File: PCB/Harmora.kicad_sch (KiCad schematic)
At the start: 14 parts, among them U14 ATmega328p-AU, U17 128x64 2.42 inc, Y1 16Mhz

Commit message: new schematics
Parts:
- added C50: 100nF, Footprints:0603_C, symbol Symbols:Capacitor 0603
- added FB1: 600Ω@100MHz, Footprints:0603_FB, symbol Symbols:Ferrite_beat
- C44, C45, C46, C47, C48: footprint (none) -> Footprints:0603_C
- C49: value 12pF -> 100nF; footprint (none) -> Footprints:0603_C
- R10, R11, R12, R13, R9: footprint (none) -> Footprints:0603_R
- U14: footprint (none) -> Footprints:ATMEGA328P-AU
- U17: footprint (none) -> Footprints:SPI Screen PinHeader
- Y1: footprint (none) -> Footprints:Crystal Oscillator 16MHz
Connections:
- net GND: now also C49.1, C50.1
- net VCC: now also FB1.1; no longer C45.2, C46.2, C49.1, U14.18 (AVCC), U14.4 (VCC)
- new net: C45.2, C46.2, FB1.2, U14.18 (AVCC)
- new net: C50.2, U14.4 (VCC)
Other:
- sheet ATmega32u4: file MCU_32u4.kicad_sch -> schematic_pages/MCU_32u4.kicad_sch
- note added: "Crystal oscilator"
- note removed: "Crystal"
- moved on the sheet: C45, C46, C47, C48, C49, Y1

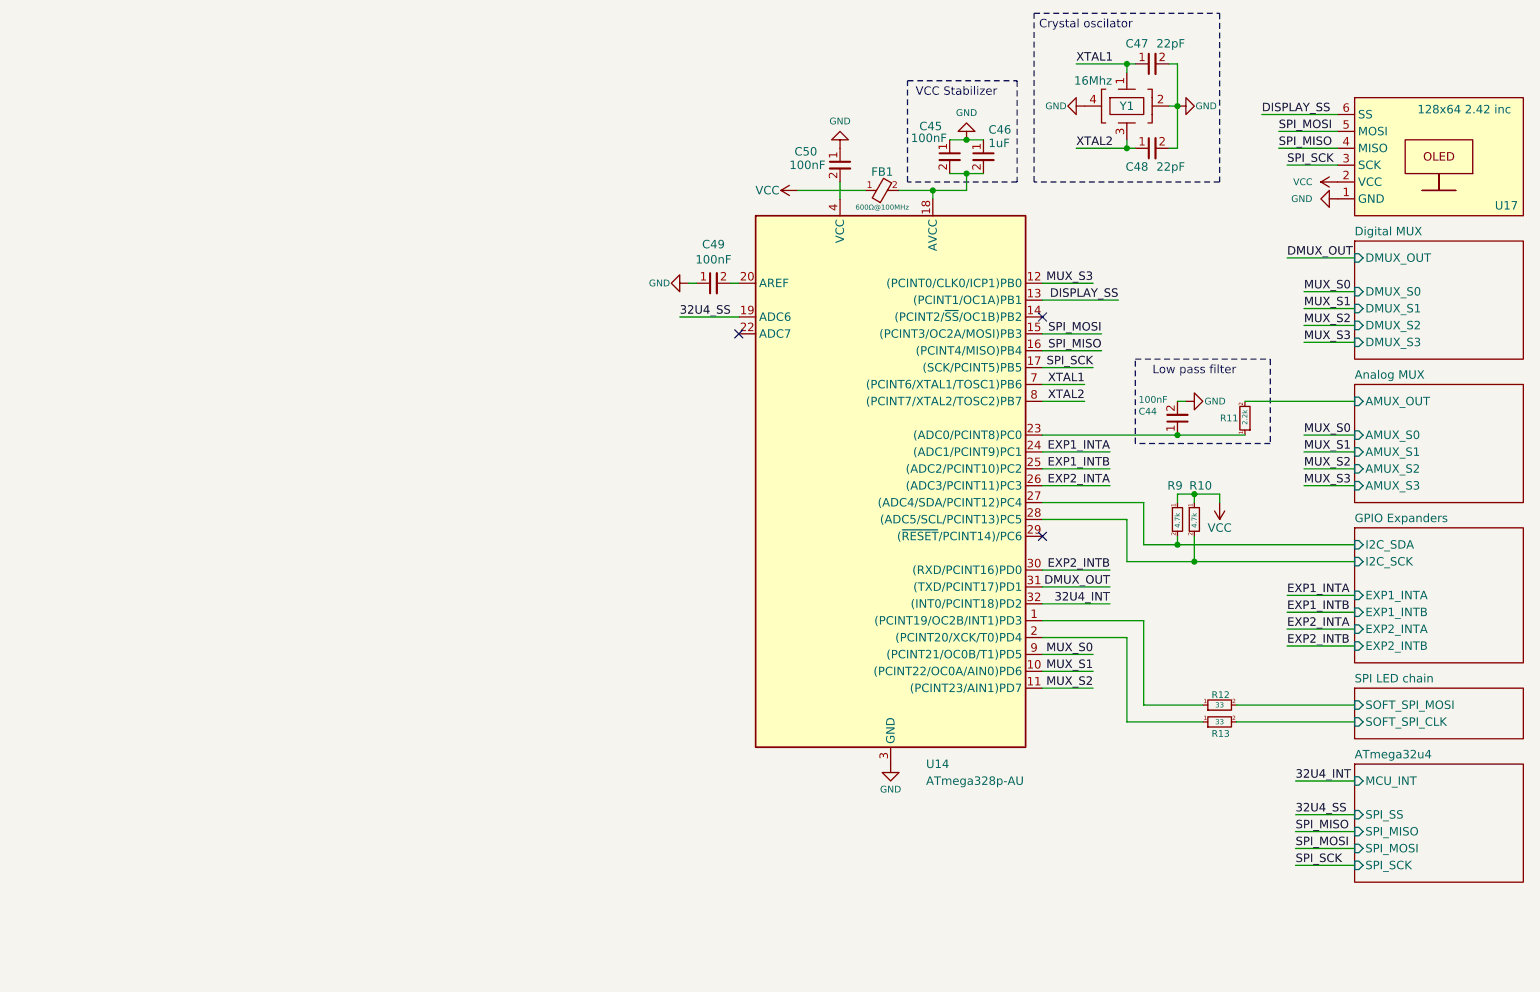
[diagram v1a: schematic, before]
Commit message: ISP ports, RESET lines, MIDI DIN 5
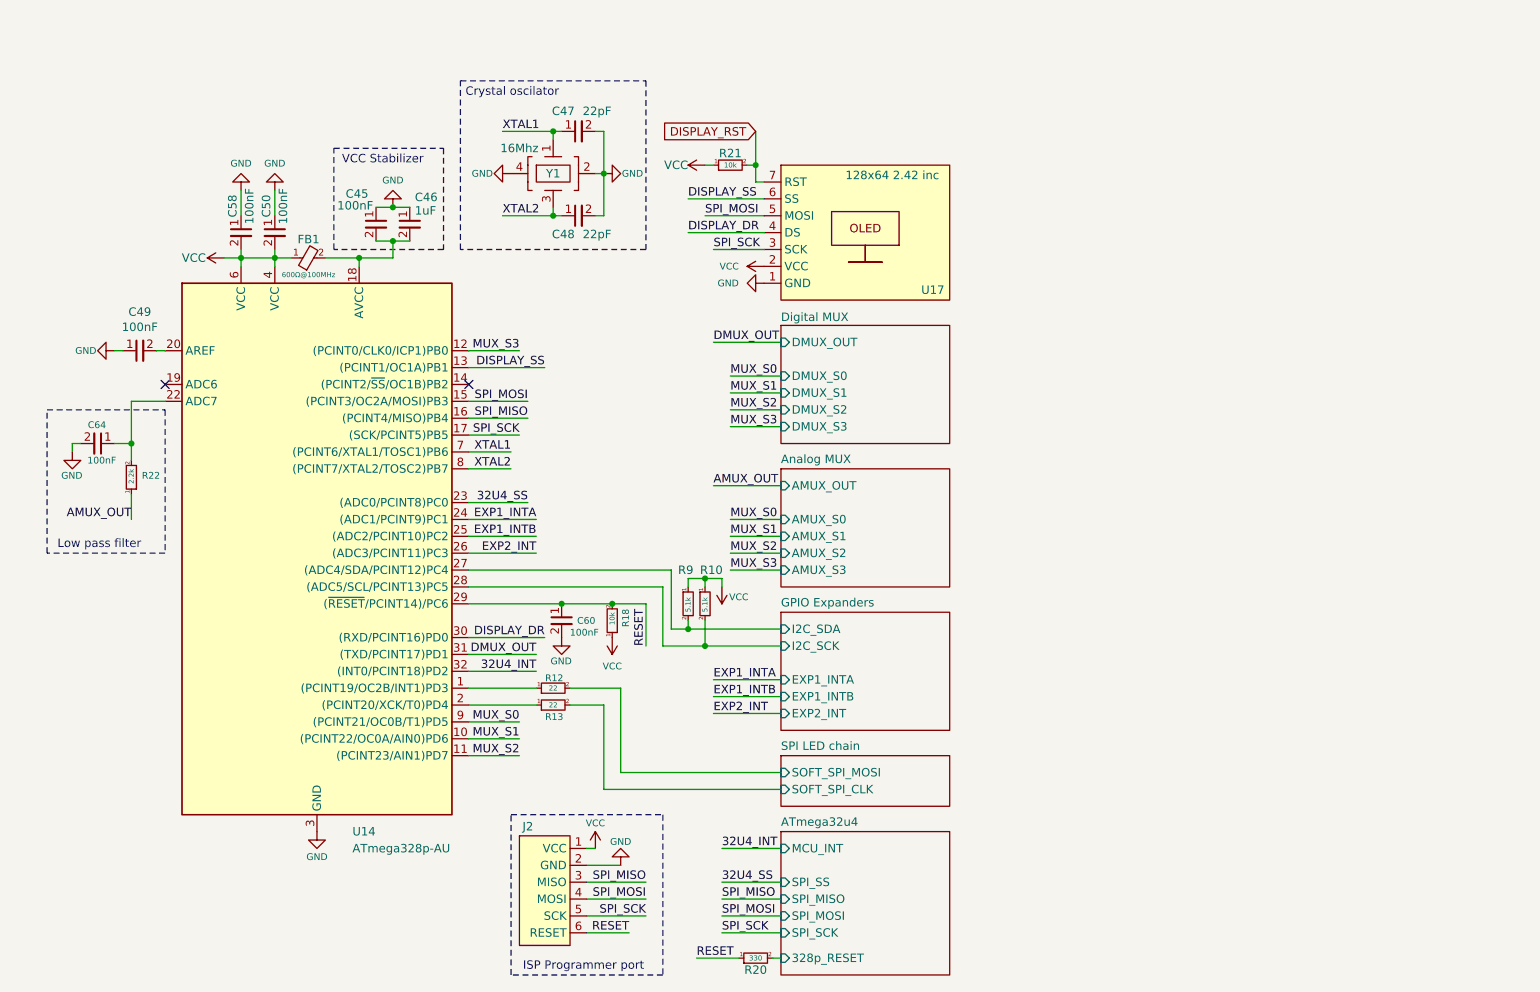
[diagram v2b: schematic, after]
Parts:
- removed C44: 100nF, Footprints:0603_C, symbol Symbols:Capacitor 0603
- removed R11: 2.2k, Footprints:0603_R, symbol Symbols:Resistor 0603
- added C58, C60, C64: 100nF, Footprints:0603_C, symbol Symbols:Capacitor 0603
- added J2: ~, Footprints:ISP port, symbol Symbols:ISP_Port
- added R18, R21: 10k, Footprints:0603_R, symbol Symbols:Resistor 0603
- added R20: 330, Footprints:0603_R, symbol Symbols:Resistor 0603
- added R22: 2.2k, Footprints:0603_R, symbol Symbols:Resistor 0603
- R10, R9: value 4.7k -> 5.1k
- R12, R13: value 33 -> 22
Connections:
- net 32U4_SS: now also U14.23 ((ADC0/PCINT8)PC0); no longer U14.19 (ADC6)
- net GND: now also C58.1, C60.2, C64.2, J2.2 (GND)
- net SPI_MISO: now also J2.3 (MISO); no longer U17.4 (MISO)
- net SPI_MOSI: now also J2.4 (MOSI)
- net SPI_SCK: now also J2.5 (SCK)
- net VCC: now also C50.2, U14.4 (VCC), U14.6 (VCC), C58.2, J2.1 (VCC), R18.1, R21.1
- net at U14.22 (ADC7): now also C64.1, R22.2
- net RESET: now reaches U14.29 ((~{RESET}/PCINT14)/PC6)
- net RESET: now also C60.1, J2.6 (RESET), R18.2, R20.1
- net EXP2_INTA renamed EXP2_INT
- net EXP2_INTB renamed DISPLAY_DR
- net DISPLAY_DR: now also U17.4 (DS)
- new net AMUX_OUT: R22.1
- new net ATmega32u4/328p_RESET: R20.2
- new net DISPLAY_RST: R21.2, U17.7 (RST)
- no-connect marks 3 -> 2
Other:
- sheet ATmega32u4 ports: added 328p_RESET; removed none
- sheet GPIO Expanders ports: added EXP2_INT; removed EXP2_INTA, EXP2_INTB
- note added: "ISP Programmer port"
- moved on the sheet: C45, C46, C47, C48, C49, C50, FB1, R10, R12, R13, R9, Y1

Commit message: led chain
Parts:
- renumbered U17 to J5
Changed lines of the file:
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@@
 		(on_board yes)
 		(dnp no)
-		(property "Reference" "U17"
+		(property "Reference" "J5"
 			(at 152.4 63.246 0)
 			(effects
@@
 			(project "MCU_328p"
 				(path "/de43e009-b04c-42c1-b131-cdc664039a0d"
-					(reference "U17")
+					(reference "J5")
 					(unit 1)
 				)

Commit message: pcb: piano done
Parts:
- renumbered C46 to C73, C47 to C79, C48 to C80, R12 to R10, R13 to R11, R18 to R14, R21 to R16, R20 to R17, R22 to R5, R9 to R6, R10 to R7
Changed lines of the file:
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@@
 		(on_board yes)
 		(dnp no)
-		(property "Reference" "R13"
+		(property "Reference" "R11"
 			(at 96.774 127.508 90)
 			(effects
@@
 			(project "pcb_schematics"
 				(path "/de43e009-b04c-42c1-b131-cdc664039a0d"
-					(reference "R13")
+					(reference "R11")
 					(unit 1)
 				)
@@
 		(on_board yes)
 		(dnp no)
-		(property "Reference" "C47"
+		(property "Reference" "C79"
 			(at 96.774 36.322 90)
 			(effects
@@
 			(project ""
 				(path "/de43e009-b04c-42c1-b131-cdc664039a0d"
-					(reference "C47")
+					(reference "C79")
 					(unit 1)
 				)
@@
 		(on_board yes)
 		(dnp no)
-		(property "Reference" "C48"
+		(property "Reference" "C80"
 			(at 96.774 54.864 90)
 			(effects
@@
 			(project "MCU_328p"
 				(path "/de43e009-b04c-42c1-b131-cdc664039a0d"
-					(reference "C48")
+					(reference "C80")
 					(unit 1)
 				)
@@
 		(on_board yes)
 		(dnp no)
-		(property "Reference" "C46"
+		(property "Reference" "C73"
 			(at 74.422 49.2822 0)
 			(effects
@@
 			(project "pcb_schematics"
 				(path "/de43e009-b04c-42c1-b131-cdc664039a0d"
-					(reference "C46")
+					(reference "C73")
 					(unit 1)
 				)
@@
 		(on_board yes)
 		(dnp no)
-		(property "Reference" "R12"
+		(property "Reference" "R10"
 			(at 96.774 121.666 90)
 			(effects
@@
 			(project "pcb_schematics"
 				(path "/de43e009-b04c-42c1-b131-cdc664039a0d"
-					(reference "R12")
+					(reference "R10")
 					(unit 1)
 				)
@@
 		(on_board yes)
 		(dnp no)
-		(property "Reference" "R10"
+		(property "Reference" "R7"
 			(at 117.348 105.41 0)
 			(effects
@@
 			(project "pcb_schematics"
 				(path "/de43e009-b04c-42c1-b131-cdc664039a0d"
-					(reference "R10")
+					(reference "R7")
 					(unit 1)
 				)
@@
 		(on_board yes)
 		(dnp no)
-		(property "Reference" "R18"
+		(property "Reference" "R14"
 			(at 106.172 111.252 90)
 			(effects
@@
 			(project "Harmora"
 				(path "/de43e009-b04c-42c1-b131-cdc664039a0d"
-					(reference "R18")
+					(reference "R14")
 					(unit 1)
 				)
@@
 		(on_board yes)
 		(dnp no)
-		(property "Reference" "R20"
+		(property "Reference" "R17"
 			(at 125.73 165.608 90)
 			(effects
@@
 			(project "Harmora"
 				(path "/de43e009-b04c-42c1-b131-cdc664039a0d"
-					(reference "R20")
+					(reference "R17")
 					(unit 1)
 				)
@@
 		(on_board yes)
 		(dnp no)
-		(property "Reference" "R22"
-			(at 36.068 91.186 0)
+		(property "Reference" "R5"
+			(at 35.052 91.44 0)
 			(effects
 				(font
@@
 			(project "Harmora"
 				(path "/de43e009-b04c-42c1-b131-cdc664039a0d"
-					(reference "R22")
+					(reference "R5")
 					(unit 1)
 				)
@@
 		(on_board yes)
 		(dnp no)
-		(property "Reference" "R9"
+		(property "Reference" "R6"
 			(at 114.046 105.41 0)
 			(effects
@@
 			(project ""
 				(path "/de43e009-b04c-42c1-b131-cdc664039a0d"
-					(reference "R9")
+					(reference "R6")
 					(unit 1)
 				)
@@
 		(on_board yes)
 		(dnp no)
-		(property "Reference" "R21"
+		(property "Reference" "R16"
 			(at 121.92 42.672 90)
 			(effects
@@
 			(project ""
 				(path "/de43e009-b04c-42c1-b131-cdc664039a0d"
-					(reference "R21")
-					(unit 1)
-				)
+					(reference "R16")
+					(unit 1)
+				)

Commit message: pc is being
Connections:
- net EXP1_INTA: now also U14.25 ((ADC2/PCINT10)PC2); no longer U14.24 ((ADC1/PCINT9)PC1)
- net EXP1_INTB: now also U14.24 ((ADC1/PCINT9)PC1); no longer U14.25 ((ADC2/PCINT10)PC2)
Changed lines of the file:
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@@
+	(wire
+		(pts
+			(xy 82.55 100.33) (xy 92.71 100.33)
+		)
+		(stroke
+			(width 0)
+			(type default)
+		)
+	)
 	(wire
 		(pts
@@
 	(wire
 		(pts
+			(xy 82.55 97.79) (xy 92.71 97.79)
+		)
+		(stroke
+			(width 0)
+			(type default)
+		)
+	)
+	(wire
+		(pts
 			(xy 82.55 85.09) (xy 90.17 85.09)
 		)
@@
 	(wire
 		(pts
-			(xy 82.55 100.33) (xy 92.71 100.33)
-		)
-		(stroke
-			(width 0)
-			(type default)
-		)
-	)
-	(wire
-		(pts
 			(xy 82.55 110.49) (xy 96.52 110.49)
 		)
@@
 		(pts
 			(xy 87.63 52.07) (xy 95.25 52.07)
-		)
-		(stroke
-			(width 0)
-			(type default)
-		)
-	)
-	(wire
-		(pts
-			(xy 82.55 97.79) (xy 92.71 97.79)
 		)
 		(stroke
@@
 	)
 	(label "EXP1_INTB"
-		(at 92.71 100.33 180)
+		(at 92.71 97.79 180)
 		(effects
 			(font
@@
 	)
 	(label "EXP1_INTA"
-		(at 92.71 97.79 180)
-		(effects
-			(font
+		(at 92.71 100.33 180)
+		(effects
+			(font

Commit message: PCB V1.0 DONE
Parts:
- removed C58: 100nF, Footprints:0603_C, symbol Symbols:Capacitor 0603
- added R17, R18: 10k, Footprints:0603_R, symbol Symbols:Resistor 0603
- renumbered R17 to R19
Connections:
- net DISPLAY_SS: now also U14.1 ((PCINT19/OC2B/INT1)PD3), R18.2; no longer U14.13 ((PCINT1/OC1A)PB1)
- net MUX_S3: now also U14.2 ((PCINT20/XCK/T0)PD4); no longer U14.12 ((PCINT0/CLK0/ICP1)PB0)
- net VCC: now also R17.2, R18.1
- net at R11.1: now also U14.13 ((PCINT1/OC1A)PB1); no longer U14.2 ((PCINT20/XCK/T0)PD4)
- net at R10.1: now also U14.12 ((PCINT0/CLK0/ICP1)PB0); no longer U14.1 ((PCINT19/OC2B/INT1)PD3)
- net at U14.14 ((PCINT2/~{SS}/OC1B)PB2): now also R17.1
- net SPI LED chain/SOFT_SPI_CLK renamed SOFT_SPI_CLK
- net SPI LED chain/SOFT_SPI_MOSI renamed SOFT_SPI_MOSI
- no-connect marks 2 -> 1
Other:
- moved on the sheet: C50, C79, C80, R10, R11, R16, Y1

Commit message: last double-checks
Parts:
- renumbered C64 to C13
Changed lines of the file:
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@@
 		(on_board yes)
 		(dnp no)
-		(property "Reference" "C64"
+		(property "Reference" "C13"
 			(at 27.94 83.566 90)
 			(effects
@@
 			(project "Harmora"
 				(path "/de43e009-b04c-42c1-b131-cdc664039a0d"
-					(reference "C64")
+					(reference "C13")
 					(unit 1)
 				)
